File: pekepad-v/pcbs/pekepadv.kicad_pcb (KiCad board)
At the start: 2 copper layers, 78 x 128.2 mm, 45 parts

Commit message: switchplate fix
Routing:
- net P024: track 225.6 -> 110.6 mm
- net P022: track 132.6 -> 117.8 mm, vias 3 -> 4
- net P113: track 126.4 -> 136.5 mm
- net P115: track 107.0 -> 116.5 mm, vias 0 -> 1
- net RAW: track 59.8 -> 50.6 mm, vias 1 -> 0
- net P029: track 228.8 -> 222.4 mm, vias 3 -> 2
- net P008: track 119.5 -> 113.6 mm, vias 4 -> 1
- net P111: track 118.2 -> 123.4 mm
- net P006: track 42.8 -> 38.6 mm, vias 0 -> 1
- net right-outer_bottom: track 16.8 -> 13.6 mm
- net middle_top: track 13.6 -> 15.2 mm
- net P031: track 97.0 -> 95.4 mm
- net P106: track 99.0 -> 100.1 mm
- net P010: track 16.6 -> 17.8 mm
- net P002: track 107.1 -> 106.4 mm, vias 2 -> 1
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
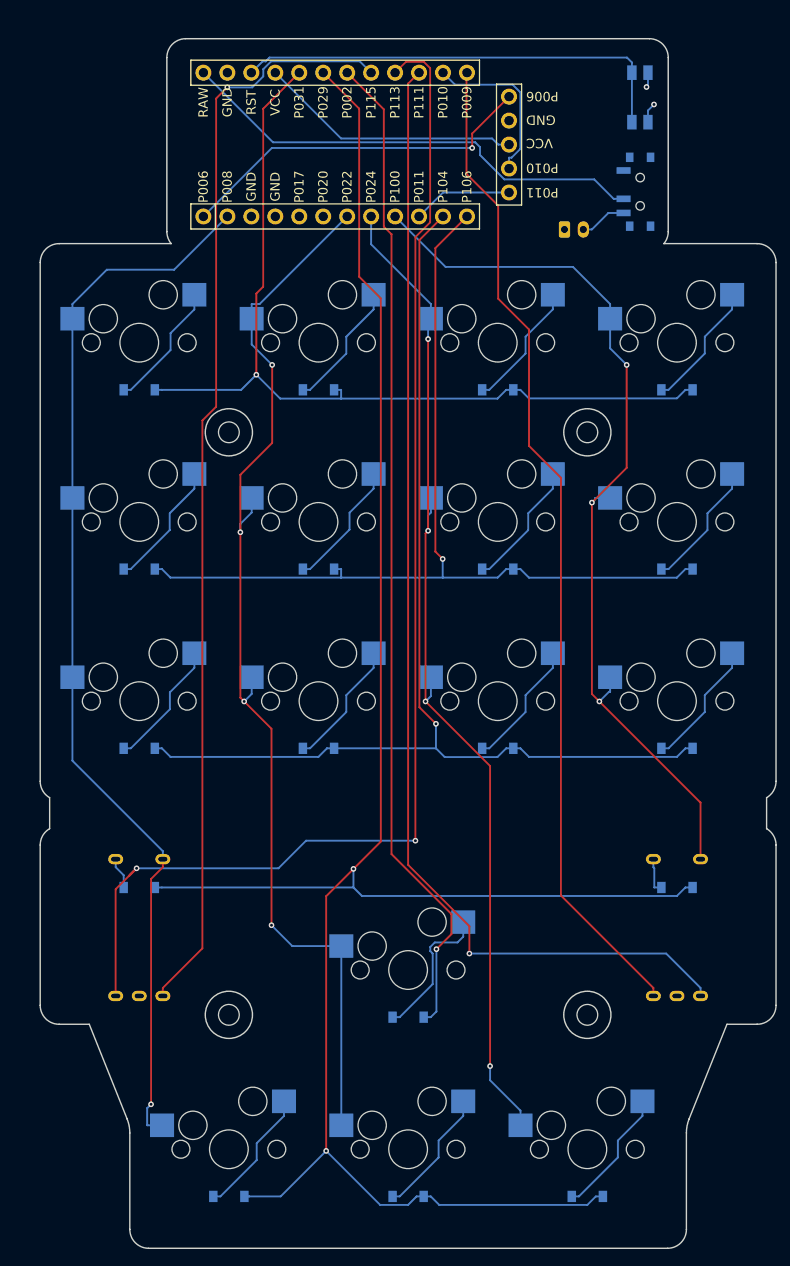
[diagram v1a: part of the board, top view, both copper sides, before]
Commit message: Moving battery connector to Front
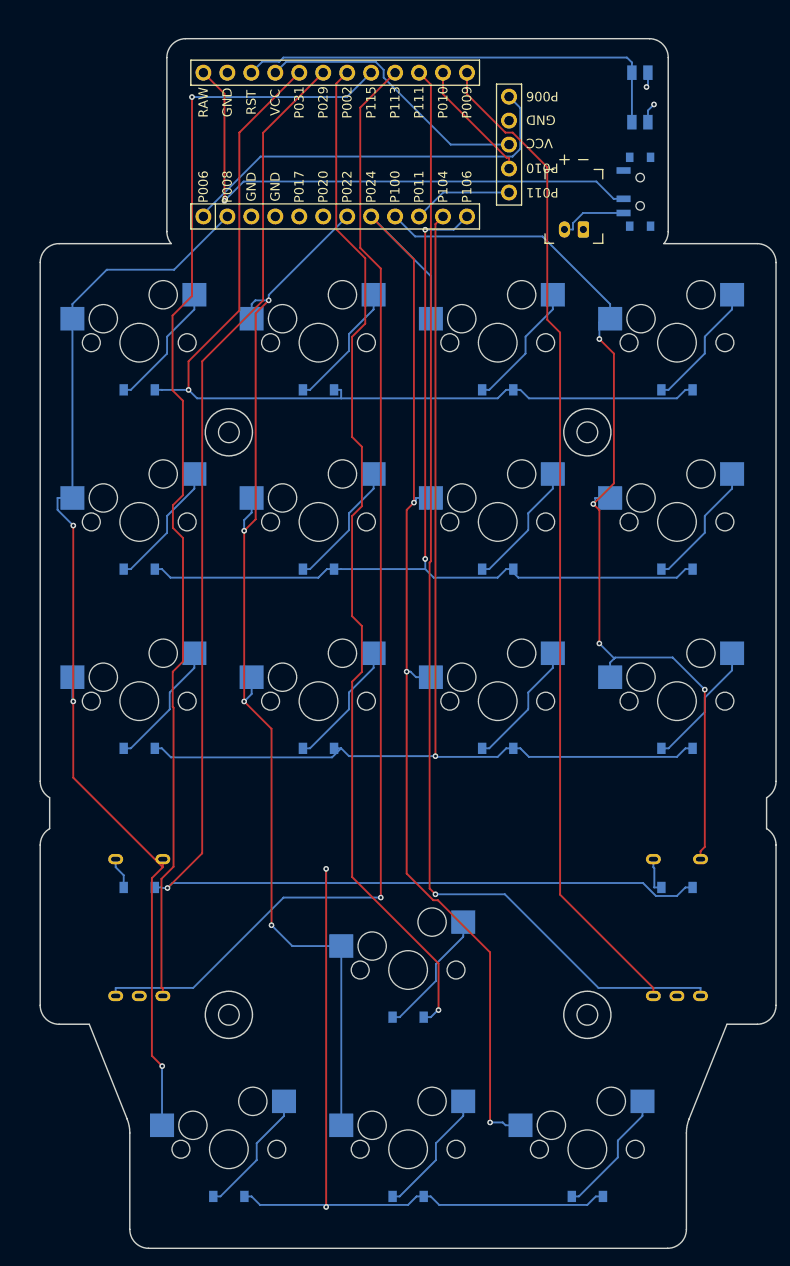
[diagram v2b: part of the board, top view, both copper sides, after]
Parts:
- JST1: moved to F.Cu
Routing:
- net P113: track 136.5 -> 122.8 mm, vias 2 -> 1
- net P024: track 110.6 -> 124.0 mm, vias 4 -> 3
- net RAW: track 50.6 -> 58.4 mm, vias 0 -> 1
- net P029: track 222.4 -> 228.5 mm, vias 2 -> 3
- net P010: track 17.8 -> 13.2 mm
- net P008: track 113.6 -> 117.9 mm, vias 1 -> 3
- net P006: track 38.6 -> 42.8 mm, vias 1 -> 0
- net P100: track 97.8 -> 101.6 mm, vias 3 -> 4
- net P031: track 95.4 -> 98.6 mm
- net P002: track 106.4 -> 109.1 mm
- net P111: track 123.4 -> 121.0 mm
- net BAT_P: track 4.99 -> 7.39 mm
- net P115: track 116.5 -> 118.7 mm
- net middle_top: track 15.2 -> 13.6 mm
- net VCC: track 27.9 -> 29.4 mm
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
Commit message: Removing right side for Cases section
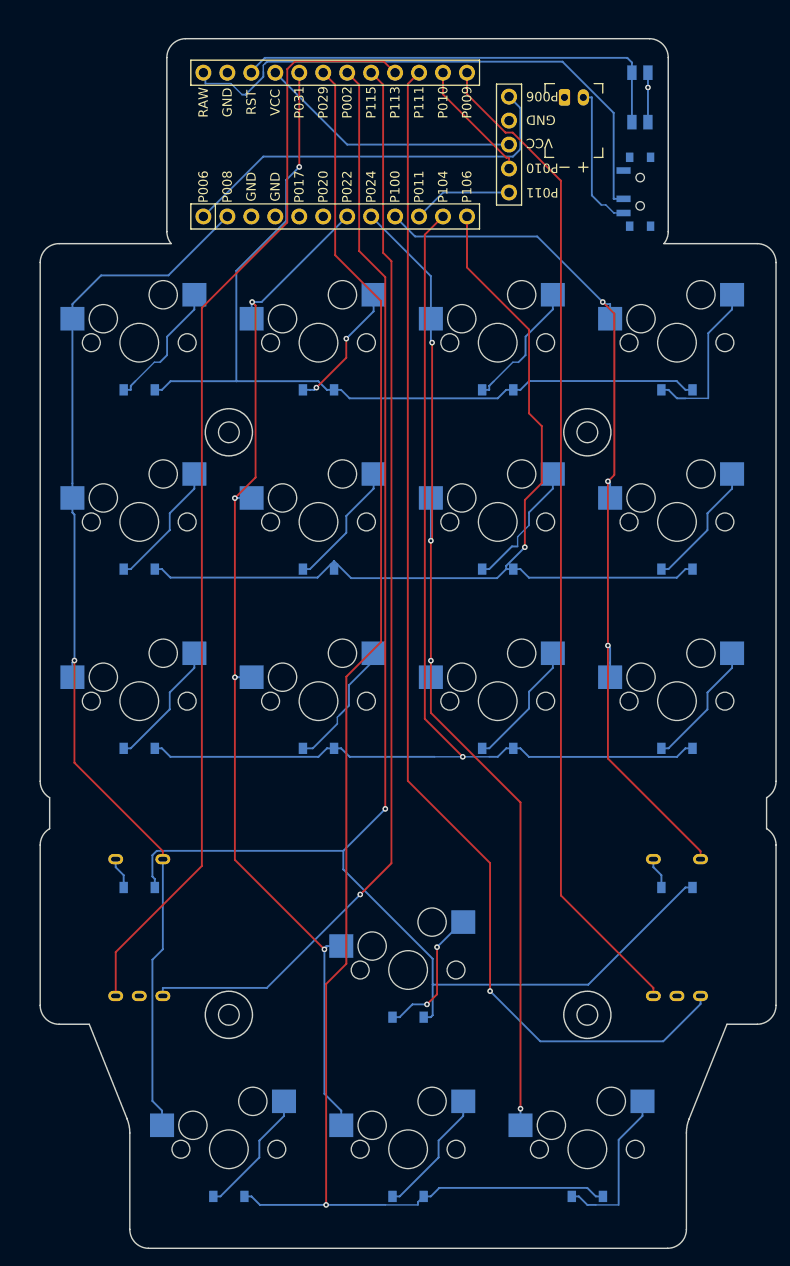
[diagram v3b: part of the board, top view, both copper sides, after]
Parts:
- moved JST1 14.0 mm to (146.1, 56.0), turned to 0 degrees
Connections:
- D17 pad 1: P029 -> P002
- D18 pad 1: P029 -> P002
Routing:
- net P029: track 228.5 -> 164.6 mm, vias 3 -> 1
- net P002: track 109.1 -> 164.2 mm
- net P024: track 124.0 -> 109.3 mm, vias 3 -> 4
- net BAT_P: track 7.39 -> 15.4 mm
- net P111: track 121.0 -> 128.5 mm
- net P113: track 122.8 -> 118.0 mm, vias 1 -> 0
- net P022: track 118.4 -> 114.2 mm
- net P100: track 101.6 -> 97.4 mm, vias 4 -> 3
- net P008: track 117.9 -> 114.0 mm, vias 3 -> 1
- net P031: track 98.6 -> 94.7 mm
- net right_bottom: track 13.6 -> 17.4 mm
- net right-outer_top: track 13.6 -> 17.4 mm
- net P115: track 118.7 -> 115.3 mm
- net P106: track 100.6 -> 103.1 mm, vias 2 -> 1
- net GND: track 3.73 -> 5.25 mm, vias 2 -> 1
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
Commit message: JLCPCB fabrication ready
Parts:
- moved DISP1 3.00 mm to (119.5, 61.0)
- moved JST1 3.00 mm to (149.1, 56.0)
- moved MCU1 3.00 mm to (116.5, 61.0)
- moved PWR1 3.00 mm to (156.1, 66.0)
- moved RST1 3.00 mm to (156.1, 56.0)
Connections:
- D1 pad 1: P104 -> P011
- D10 pad 1: P104 -> P011
- D11 pad 1: P106 -> P100
- D12 pad 1: P031 -> P024
- D13 pad 1: P029 -> P009
- D14 pad 1: P029 -> P009
- D15 pad 1: P002 -> P104
- D16 pad 1: P029 -> P009
- D17 pad 1: P002 -> P104
- D18 pad 1: P002 -> P104
- D2 pad 1: P106 -> P100
- D3 pad 1: P031 -> P024
- D4 pad 1: P104 -> P011
- D5 pad 1: P106 -> P100
- D6 pad 1: P031 -> P024
- D7 pad 1: P104 -> P011
- D8 pad 1: P106 -> P100
- D9 pad 1: P031 -> P024
- DISP1 pad 1: P011 -> P017
- DISP1 pad 2: P010 -> P020
- RE1 pad A: P115 -> P022
- RE1 pad C: P113 -> P008
- RE1 pad S2: P008 -> P031
- RE2 pad A: P111 -> P110
- RE2 pad C: P009 -> P106
- RE2 pad S2: P100 -> P115
- S1 pad 1: P008 -> P031
- S10 pad 1: P100 -> P115
- S11 pad 1: P100 -> P115
- S12 pad 1: P100 -> P115
- S13 pad 1: P008 -> P031
- S14 pad 1: P022 -> P029
- S15 pad 1: P022 -> P029
- S16 pad 1: P024 -> P002
- S2 pad 1: P008 -> P031
- S3 pad 1: P008 -> P031
- S4 pad 1: P022 -> P029
- S5 pad 1: P022 -> P029
- S6 pad 1: P022 -> P029
- S7 pad 1: P024 -> P002
- S8 pad 1: P024 -> P002
- S9 pad 1: P024 -> P002
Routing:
- net P111: track 128.5 -> 0.00 mm, vias 1 -> 0
- net P113: track 118.0 -> 0.00 mm
- net P011: track 10.6 -> 117.2 mm, vias 0 -> 1
- net P009: track 106.5 -> 161.9 mm, vias 0 -> 1
- net P104: track 119.0 -> 167.0 mm
- net P002: track 164.2 -> 126.2 mm, vias 1 -> 5
- net P031: track 94.7 -> 131.2 mm
- net P029: track 164.6 -> 129.5 mm, vias 1 -> 4
- net P024: track 109.3 -> 80.2 mm, vias 4 -> 0
- net P008: track 114.0 -> 86.5 mm, vias 1 -> 0
- net P017: track 0.00 -> 24.7 mm
- net P022: track 114.2 -> 91.8 mm, vias 4 -> 0
- net P020: track 0.00 -> 21.8 mm
- net RST: track 47.6 -> 69.3 mm
- net P010: track 13.2 -> 0.00 mm
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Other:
- outline, holes or cut-outs redrawn
- board text added: "Pekepad-v v1.0 by pedroren"
